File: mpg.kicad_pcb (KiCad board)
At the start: 2 copper layers, 50.3 x 100.1 mm, 60 parts, among them J1 Conn_01x04_Male, J2 DB25_Male_MountingHoles, J3 Conn_01x03_Male, J7 RJ45_Shielded, K1 G5LE-1, Q1 BC847, Q2 BC847, Q3 BC847, Q4 BC847, Q5 BC847, SW1 SW_Push, U1 LD2981ABU33TR, U2 STM32G031F4Px, U3 SP3485CN

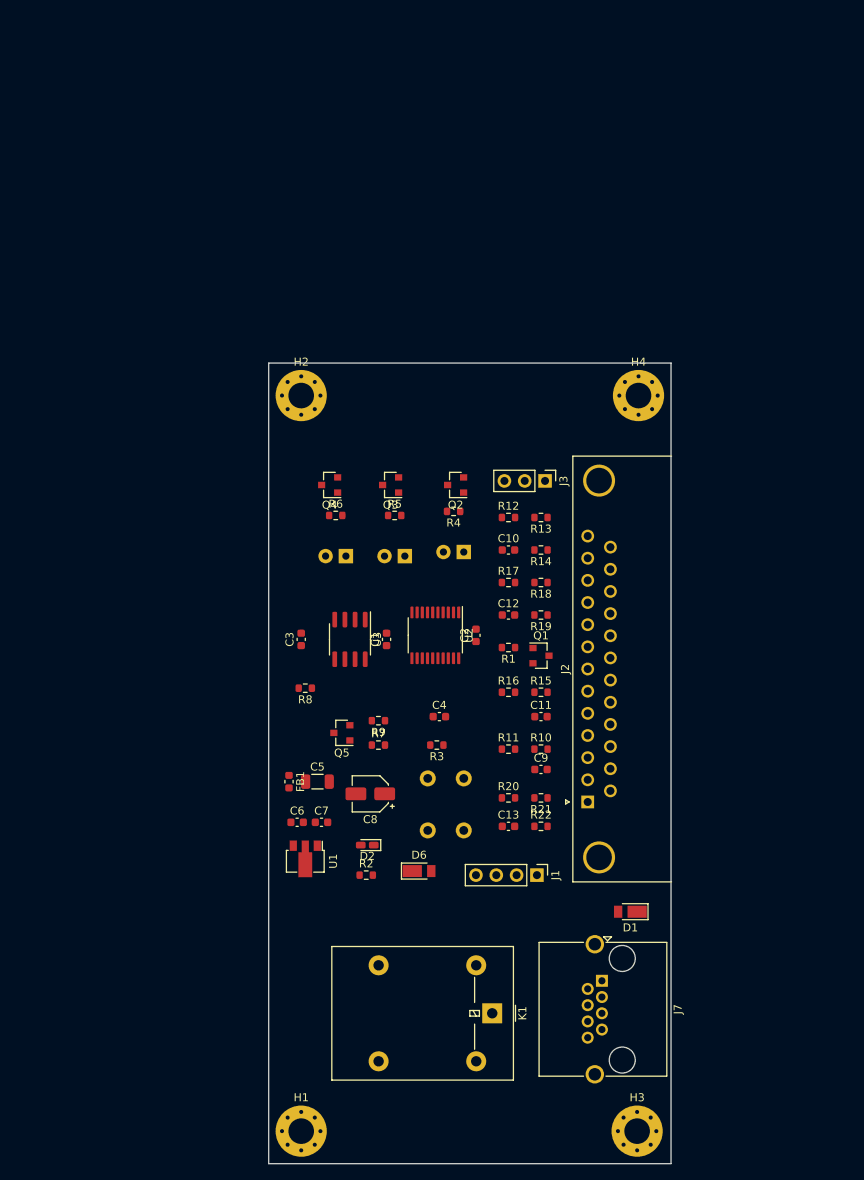
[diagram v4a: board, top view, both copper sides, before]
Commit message: Redesigned around G431.
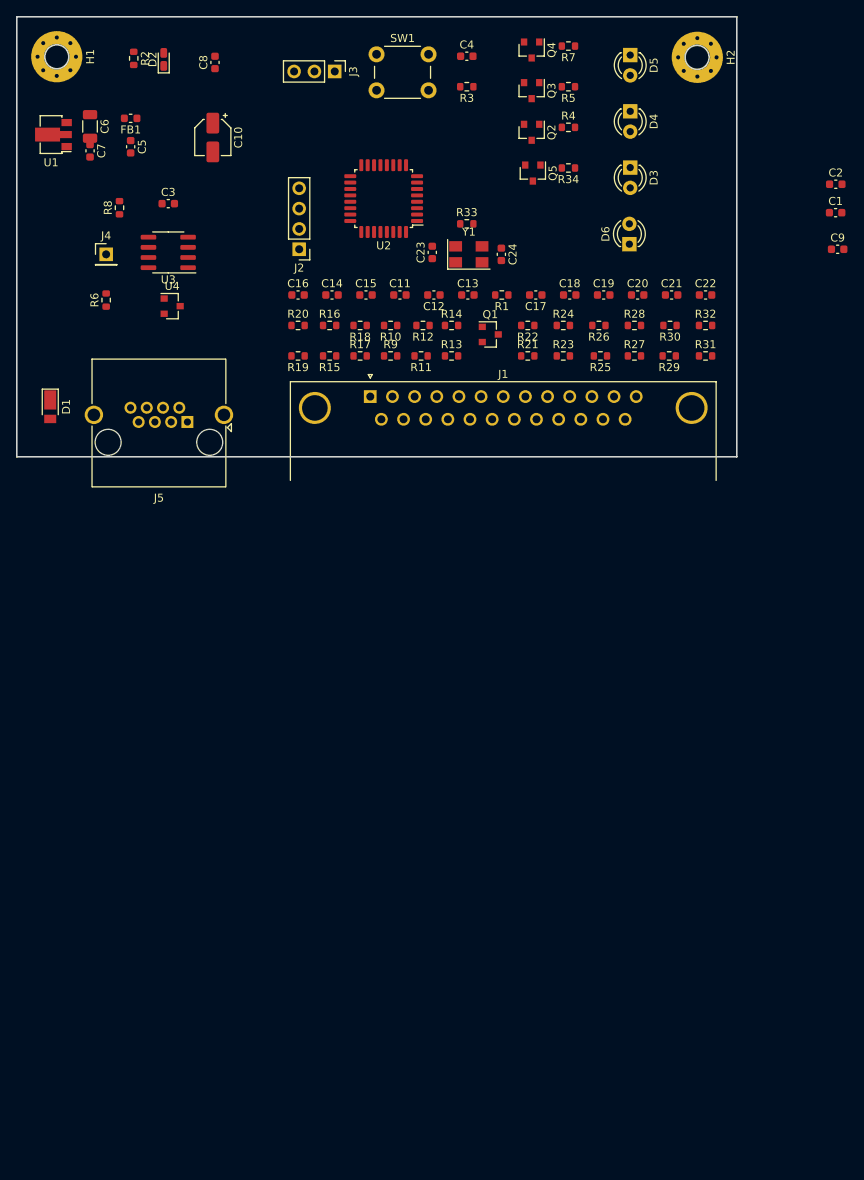
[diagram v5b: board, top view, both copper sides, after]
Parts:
- removed H3, H4: MountingHole_Pad, MountingHole:MountingHole_3.2mm_M3_Pad_Via
- removed J7: RJ45_Shielded, Connector_RJ:RJ45_Amphenol_RJHSE5380
- removed K1: G5LE-1, Relay_THT:Relay_SPDT_Omron-G5LE-1
- added C14: 10n, Capacitor_SMD:C_0603_1608Metric, F.Cu at (127.3, 88.5)
- added C15: 10n, Capacitor_SMD:C_0603_1608Metric, F.Cu at (131.5, 88.5)
- added C16: 10n, Capacitor_SMD:C_0603_1608Metric, F.Cu at (123.0, 88.5)
- added C17: 10n, Capacitor_SMD:C_0603_1608Metric, F.Cu at (152.8, 88.5)
- added C18: 10n, Capacitor_SMD:C_0603_1608Metric, F.Cu at (157.0, 88.5)
- added C19: 10n, Capacitor_SMD:C_0603_1608Metric, F.Cu at (161.3, 88.5)
- added C20: 10n, Capacitor_SMD:C_0603_1608Metric, F.Cu at (165.5, 88.5)
- added C21: 10n, Capacitor_SMD:C_0603_1608Metric, F.Cu at (169.7, 88.5)
- added C22: 10n, Capacitor_SMD:C_0603_1608Metric, F.Cu at (174.0, 88.5)
- added C23: 27p, Capacitor_SMD:C_0603_1608Metric, F.Cu at (139.8, 83.2)
- added C24: 27p, Capacitor_SMD:C_0603_1608Metric, F.Cu at (148.5, 83.4)
- added J4: Conn_01x02_Male, Connector_PinHeader_2.54mm:PinHeader_1x01_P2.54mm_Vertical, F.Cu at (99.1, 83.4)
- added J5: RJ45_Shielded, Connector_RJ:RJ45_Amphenol_RJHSE5380, F.Cu at (109.2, 104.4)
- added R23: 10k, Resistor_SMD:R_0603_1608Metric, F.Cu at (156.2, 96.1)
- added R24: 10k, Resistor_SMD:R_0603_1608Metric, F.Cu at (156.2, 92.3)
- added R25: 10k, Resistor_SMD:R_0603_1608Metric, F.Cu at (160.8, 96.1)
- added R26: 10k, Resistor_SMD:R_0603_1608Metric, F.Cu at (160.7, 92.3)
- added R27: 10k, Resistor_SMD:R_0603_1608Metric, F.Cu at (165.1, 96.1)
- added R28: 10k, Resistor_SMD:R_0603_1608Metric, F.Cu at (165.1, 92.3)
- added R29: 10k, Resistor_SMD:R_0603_1608Metric, F.Cu at (169.4, 96.1)
- added R30: 10k, Resistor_SMD:R_0603_1608Metric, F.Cu at (169.5, 92.3)
- added R31: 10k, Resistor_SMD:R_0603_1608Metric, F.Cu at (174.0, 96.1)
- added R32: 10k, Resistor_SMD:R_0603_1608Metric, F.Cu at (174.0, 92.3)
- added R33: 470, Resistor_SMD:R_0603_1608Metric, F.Cu at (144.1, 79.6)
- added R34: 47, Resistor_SMD:R_0603_1608Metric, F.Cu at (156.8, 72.6)
- added U4: ESDCAN24-2BLY, Package_TO_SOT_SMD:SOT-23, F.Cu at (107.3, 89.9)
- added Y1: 8MHz, Crystal:Crystal_SMD_5032-4Pin_5.0x3.2mm, F.Cu at (144.4, 83.4)
- C10: value 10n -> 10u; footprint Capacitor_SMD:C_0603_1608Metric -> Capacitor_SMD:CP_Elec_4x5.8
- C5: value 22u -> 100n; footprint Capacitor_SMD:C_1206_3216Metric -> Capacitor_SMD:C_0603_1608Metric
- C6: value 100n -> 22u; footprint Capacitor_SMD:C_0603_1608Metric -> Capacitor_SMD:C_1206_3216Metric
- C8: value 10u -> 100n; footprint Capacitor_SMD:CP_Elec_4x5.8 -> Capacitor_SMD:C_0603_1608Metric
- C9: value 10n -> 100n
- D3, D4, D5, SW1: moved to F.Cu
- D6: value D -> LED; footprint Diode_SMD:D_PowerDI-123 -> LED_THT:LED_D3.0mm
- J1: value Conn_01x04_Male -> DB25_Male_MountingHoles; footprint Connector_PinHeader_2.54mm:PinHeader_1x04_P2.54mm_Vertical -> Connector_Dsub:DSUB-25_Male_Horizontal_P2.77x2.84mm_EdgePinOffset7.70mm_Housed_MountingHolesOffset9.12mm
- J2: value DB25_Male_MountingHoles -> Conn_01x04_Male; footprint Connector_Dsub:DSUB-25_Male_Horizontal_P2.77x2.84mm_EdgePinOffset7.70mm_Housed_MountingHolesOffset9.12mm -> Connector_PinHeader_2.54mm:PinHeader_1x04_P2.54mm_Vertical
- R12, R17, R20: value 1k -> 10k
- R13, R18, R21: value 470 -> 10k
- R14, R19, R22: value 1k2 -> 10k
- R6: value 47 -> 10k
- R7: value 10k -> 47
- R8: value 220 -> 120
- U2: value STM32G031F4Px -> STM32G431K6Tx; footprint Package_SO:TSSOP-20_4.4x6.5mm_P0.65mm -> Package_QFP:LQFP-32_7x7mm_P0.8mm
- U3: value SP3485CN -> SN65HVD230
- moved H1 137.7 mm to (92.9, 58.7), turned to 270 degrees
- moved R2 106.1 mm to (102.5, 58.9), turned to 270 degrees
- moved D2 101.5 mm to (106.3, 59.1), turned to 90 degrees
- moved SW1 97.6 mm to (132.9, 58.4), turned to 0 degrees
- moved D1 96.1 mm to (92.1, 102.5), turned to 270 degrees
- moved U1 95.9 mm to (92.5, 68.5), turned to 180 degrees
- moved C8 93.5 mm to (112.7, 59.5), turned to 90 degrees
- moved C6 90.8 mm to (97.0, 67.5), turned to 270 degrees
- moved R7 90.5 mm to (156.8, 57.4), turned to 180 degrees
- moved C7 88.8 mm to (97.0, 70.5), turned to 270 degrees
- moved FB1 85.2 mm to (102.1, 66.4), turned to 180 degrees
- moved C5 82.7 mm to (102.1, 70.0), turned to 270 degrees
- moved D6 82.7 mm to (164.5, 82.2), turned to 90 degrees
- moved C4 82.6 mm to (144.1, 58.7)
- moved R3 82.4 mm to (144.1, 62.5)
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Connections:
- net A renamed CAN_L
- C1 pad 1: +3V3 -> (no net)
- C1 pad 2: GND -> (no net)
- C10 pad 1: ABC -> (no net)
- C10 pad 2: GND -> (no net)
- C11 pad 1: ENC_B -> ENC_A
- C11 pad 2: GND -> (no net)
- C12 pad 1: XYZ -> ENC_B
- C12 pad 2: GND -> (no net)
- C13 pad 1: MUL -> STOP
- C13 pad 2: GND -> (no net)
- C2 pad 1: +3V3 -> (no net)
- C2 pad 2: GND -> (no net)
- C3 pad 1: +3V3 -> (no net)
- C3 pad 2: GND -> (no net)
- C4 pad 1: RESET -> (no net)
- C4 pad 2: GND -> (no net)
- C5 pad 1: Net-(C5-Pad1) -> (no net)
- C5 pad 2: GND -> (no net)
- C6 pad 1: Net-(C5-Pad1) -> Net-(C6-Pad1)
- C6 pad 2: GND -> (no net)
- C7 pad 1: +3V3 -> RESET
- C7 pad 2: GND -> (no net)
- C8 pad 1: +3V3 -> Net-(C6-Pad1)
- C8 pad 2: GND -> (no net)
- C9 pad 1: ENC_A -> (no net)
- C9 pad 2: GND -> (no net)
- D2 pad 1: GND -> (no net)
- D3 pad 1: GND -> (no net)
- D4 pad 1: GND -> (no net)
- D5 pad 1: GND -> (no net)
- D6 pad 1: RELAY -> (no net)
- D6 pad 2: GND -> Net-(D6-Pad2)
- FB1 pad 1: Net-(C5-Pad1) -> Net-(C6-Pad1)
- H1 pad 1: GND -> (no net)
- H2 pad 1: GND -> (no net)
- J1 pad 1: GND -> (no net)
- J1 pad 2: SWCLK -> (no net)
- J1 pad 3: SWDIO -> /sheet601ED88E/In
- J1 pad 4: RESET -> /sheet601EF97F/In
- J2 pad 1: +3V3 -> (no net)
- J2 pad 2: GND -> SWCLK
- J2 pad 3: /sheet601ED88E/In -> SWDIO
- J2 pad 4: /sheet601EF97F/In -> RESET
- J3 pad 1: GND -> (no net)
- J3 pad 2: USART2_TX -> USART1_TX
- J3 pad 3: USART2_RX -> USART1_RX
- Q1 pad 2: GND -> (no net)
- Q1 pad 3: Net-(J2-Pad8) -> Net-(J1-Pad8)
- Q5 pad 1: Net-(Q5-Pad1) -> LED_D
- Q5 pad 2: GND -> Net-(Q5-Pad2)
- Q5 pad 3: STOP -> +12V
- R10 pad 1: ENC_A -> (no net)
- R10 pad 2: /sheet601ED88E/In -> ENC_A
- R11 pad 1: +3V3 -> ENC_B
- R11 pad 2: ENC_A -> /sheet601EF97F/In
- R12 pad 1: +3V3 -> (no net)
- R12 pad 2: ABC -> ENC_B
- R13 pad 1: ABC -> STOP
- R13 pad 2: /Sheet602C38D3/S2 -> /sheet60278576/In
- R14 pad 1: /Sheet602C38D3/S2 -> (no net)
- R14 pad 2: AXIS_C -> STOP
- R15 pad 1: ENC_B -> X1
- R15 pad 2: /sheet601EF97F/In -> /sheet603499BE/In
- R16 pad 1: +3V3 -> (no net)
- R16 pad 2: ENC_B -> X1
- R17 pad 1: +3V3 -> X10
- R17 pad 2: XYZ -> /sheet603603F0/In
- R18 pad 1: XYZ -> (no net)
- R18 pad 2: /sheet603130A5/S2 -> X10
- R19 pad 1: /sheet603130A5/S2 -> AXIS_C
- R19 pad 2: /sheet603130A5/S3 -> /sheet60382A0B/In
- R20 pad 1: +3V3 -> (no net)
- R20 pad 2: MUL -> AXIS_C
- R21 pad 1: MUL -> X100
- R21 pad 2: X10 -> /sheet60398AC6/In
- R22 pad 1: X10 -> (no net)
- R3 pad 1: +3V3 -> (no net)
- R6 pad 1: Net-(D5-Pad2) -> Net-(R6-Pad1)
- R6 pad 2: Net-(Q4-Pad2) -> (no net)
- R7 pad 1: Net-(Q5-Pad1) -> Net-(D5-Pad2)
- R7 pad 2: RELAY -> Net-(Q4-Pad2)
- R8 pad 1: B -> Net-(J4-Pad1)
- R9 pad 1: +3V3 -> ENC_A
- R9 pad 2: STOP -> /sheet601ED88E/In
- SW1 pad 1: GND -> (no net)
- U1 pad 1: +3V3 -> (no net)
- U1 pad 2: GND -> (no net)
- U1 pad 3: Net-(C5-Pad1) -> Net-(C6-Pad1)
- U2 pad 1: USART1_RX -> (no net)
- U2 pad 10: USART2_RX -> LED_B
- U2 pad 11: ABC -> ENC_A
- U2 pad 12: MUL -> ENC_B
- U2 pad 13: ENC_A -> LED_C
- U2 pad 14: ENC_B -> (no net)
- U2 pad 15: IND -> (no net)
- U2 pad 16: USART1_TX -> (no net)
- U2 pad 17: STOP -> (no net)
- U2 pad 18: SWDIO -> LED_D
- U2 pad 19: SWCLK -> USART1_TX
- U2 pad 2: LED_A -> Net-(C23-Pad1)
- U2 pad 20: USART1_RTS -> USART1_RX
- U2 pad 3: LED_B -> Net-(R33-Pad1)
- U2 pad 4: +3V3 -> RESET
- U2 pad 5: GND -> AXIS_Y
- U2 pad 6: RESET -> AXIS_Z
- U2 pad 7: XYZ -> AXIS_A
- U2 pad 8: LED_C -> AXIS_B
- U2 pad 9: USART2_TX -> LED_A
- U3 pad 1: USART1_RX -> FDCAN_TX
- U3 pad 2: USART1_RTS -> (no net)
- U3 pad 3: USART1_RTS -> (no net)
- U3 pad 4: USART1_TX -> FDCAN_RX
- U3 pad 5: GND -> Net-(U3-Pad5)
- U3 pad 7: B -> CAN_H
- U3 pad 8: +3V3 -> Net-(R6-Pad1)
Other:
- board size 50.3 x 100.1 mm -> 90 x 55 mm

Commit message: Minor adjustments.
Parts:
- J4: footprint Connector_PinHeader_2.54mm:PinHeader_1x01_P2.54mm_Vertical -> Connector_PinHeader_2.54mm:PinHeader_1x02_P2.54mm_Vertical
- moved C9 68.3 mm to (123.8, 68.2)
- moved C1 67.5 mm to (123.8, 66.3)
- moved C2 63.1 mm to (127.8, 66.3)
- moved C7 47.5 mm to (142.9, 58.0), turned to 180 degrees
- moved FB1 22.4 mm to (94.0, 87.2)
- moved C4 21.6 mm to (135.3, 78.4), turned to 180 degrees
- moved C5 13.6 mm to (105.4, 56.8), turned to 180 degrees
- moved R8 13.5 mm to (101.6, 91.1), turned to 270 degrees
- moved U1 13.2 mm to (103.5, 61.2), turned to 270 degrees
- moved R2 13.1 mm to (103.5, 72.0), turned to 180 degrees
- moved D1 11.6 mm to (94.0, 91.1), turned to 0 degrees
- moved C8 11.4 mm to (101.6, 56.8), turned to 0 degrees
- moved D2 10.1 mm to (103.5, 68.8), turned to 0 degrees
- moved J2 9.44 mm to (116.2, 89.2)
- moved C24 8.95 mm to (142.9, 76.5), turned to 180 degrees
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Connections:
- C1 pad 1: (no net) -> +3V3
- C1 pad 2: (no net) -> GND
- C10 pad 1: (no net) -> +3V3
- C10 pad 2: (no net) -> GND
- C11 pad 2: (no net) -> GND
- C12 pad 2: (no net) -> GND
- C13 pad 2: (no net) -> GND
- C14 pad 2: (no net) -> GND
- C15 pad 2: (no net) -> GND
- C16 pad 2: (no net) -> GND
- C17 pad 2: (no net) -> GND
- C18 pad 2: (no net) -> GND
- C19 pad 2: (no net) -> GND
- C2 pad 1: (no net) -> +3V3
- C2 pad 2: (no net) -> GND
- C20 pad 2: (no net) -> GND
- C21 pad 2: (no net) -> GND
- C22 pad 2: (no net) -> GND
- C23 pad 2: (no net) -> GND
- C24 pad 2: (no net) -> GND
- C3 pad 1: (no net) -> +3V3
- C3 pad 2: (no net) -> GND
- C4 pad 1: (no net) -> +3V3
- C4 pad 2: (no net) -> GND
- C5 pad 1: (no net) -> +3V3
- C5 pad 2: (no net) -> GND
- C6 pad 2: (no net) -> GND
- C7 pad 2: (no net) -> GND
- C8 pad 2: (no net) -> GND
- C9 pad 1: (no net) -> +3V3
- C9 pad 2: (no net) -> GND
- D2 pad 1: (no net) -> GND
- D3 pad 1: (no net) -> GND
- D4 pad 1: (no net) -> GND
- D5 pad 1: (no net) -> GND
- D6 pad 1: (no net) -> GND
- H1 pad 1: (no net) -> GND
- H2 pad 1: (no net) -> GND
- J1 pad 0: (no net) -> GND
- J1 pad 1: (no net) -> +3V3
- J1 pad 17: (no net) -> GND
- J1 pad 2: (no net) -> GND
- J1 pad 20: (no net) -> GND
- J1 pad 23: (no net) -> GND
- J1 pad 24: (no net) -> GND
- J1 pad 25: (no net) -> GND
- J2 pad 1: (no net) -> GND
- J3 pad 1: (no net) -> GND
- J5 pad 3: (no net) -> GND
- J5 pad 7: (no net) -> GND
- J5 pad SH: (no net) -> GND
- Q1 pad 2: (no net) -> GND
- R10 pad 1: (no net) -> +3V3
- R12 pad 1: (no net) -> +3V3
- R14 pad 1: (no net) -> +3V3
- R16 pad 1: (no net) -> +3V3
- R18 pad 1: (no net) -> +3V3
- R2 pad 2: +12V -> Net-(C6-Pad1)
- R20 pad 1: (no net) -> +3V3
- R22 pad 1: (no net) -> +3V3
- R24 pad 1: (no net) -> +3V3
- R26 pad 1: (no net) -> +3V3
- R28 pad 1: (no net) -> +3V3
- R3 pad 1: (no net) -> +3V3
- R30 pad 1: (no net) -> +3V3
- R32 pad 1: (no net) -> +3V3
- R6 pad 2: (no net) -> GND
- SW1 pad 1: (no net) -> GND
- U1 pad 1: (no net) -> +3V3
- U1 pad 2: (no net) -> GND
- U2 pad 1: (no net) -> +3V3
- U2 pad 14: (no net) -> GND
- U2 pad 15: (no net) -> +3V3
- U2 pad 16: (no net) -> GND
- U2 pad 17: (no net) -> +3V3
- U2 pad 32: (no net) -> GND
- U3 pad 2: (no net) -> GND
- U3 pad 3: (no net) -> +3V3
- U4 pad 3: (no net) -> GND
- Y1 pad 2: (no net) -> GND
- Y1 pad 4: (no net) -> GND

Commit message: New RJ45 footprint and layout changes.
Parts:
- J5: footprint Connector_RJ:RJ45_Amphenol_RJHSE5380 -> Local:RJ45-Wurth-615008142621
- moved C1 225.2 mm to (-92.0, 2.11)
- moved C10 225.2 mm to (-102.2, 6.55)
- moved C2 225.2 mm to (-88.1, 2.11)
- moved C23 225.2 mm to (-80.6, 16.7)
- moved C24 225.2 mm to (-73.0, 12.3)
- moved C3 225.2 mm to (-105.4, 15.4)
- moved C4 225.2 mm to (-80.6, 14.2)
- moved C5 225.2 mm to (-110.5, -7.42)
- moved C6 225.2 mm to (-121.9, 6.55)
- moved C7 225.2 mm to (-73.0, -6.15)
- moved C8 225.2 mm to (-114.3, -7.42)
- moved C9 225.2 mm to (-92.0, 4.01)
- moved D1 225.2 mm to (-121.9, 26.9)
- moved D2 225.2 mm to (-112.4, 4.65)
- moved FB1 225.2 mm to (-121.9, 23.1)
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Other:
- board size 90 x 55 mm -> 90 x 53.3 mm

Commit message: Near final layout.
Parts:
- moved R6 259.0 mm to (131.8, 80.6)
- moved U3 249.7 mm to (130.9, 74.2), turned to 270 degrees
- moved C1 249.7 mm to (149.0, 67.1)
- moved C23 249.7 mm to (160.4, 81.7)
- moved C24 249.7 mm to (168.1, 77.3)
- moved C4 249.7 mm to (160.4, 79.2)
- moved C9 249.7 mm to (149.0, 69.0)
- moved R33 249.7 mm to (164.2, 77.3)
- moved U2 249.7 mm to (154.5, 74.1)
- moved Y1 249.7 mm to (166.4, 81.7)
- moved C2 249.7 mm to (153.0, 67.1)
- moved J2 247.8 mm to (142.0, 79.8)
- moved C7 244.7 mm to (163.0, 58.6)
- moved R3 244.7 mm to (163.0, 62.4)
- moved SW1 244.0 mm to (150.4, 58.0)
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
